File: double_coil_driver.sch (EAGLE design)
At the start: 57 parts, among them Q1 MOSFET-N, Q3 IRF7493, U2 V_REG_LDOSMD, U3 LT3750EMSPBF, X1 COIL

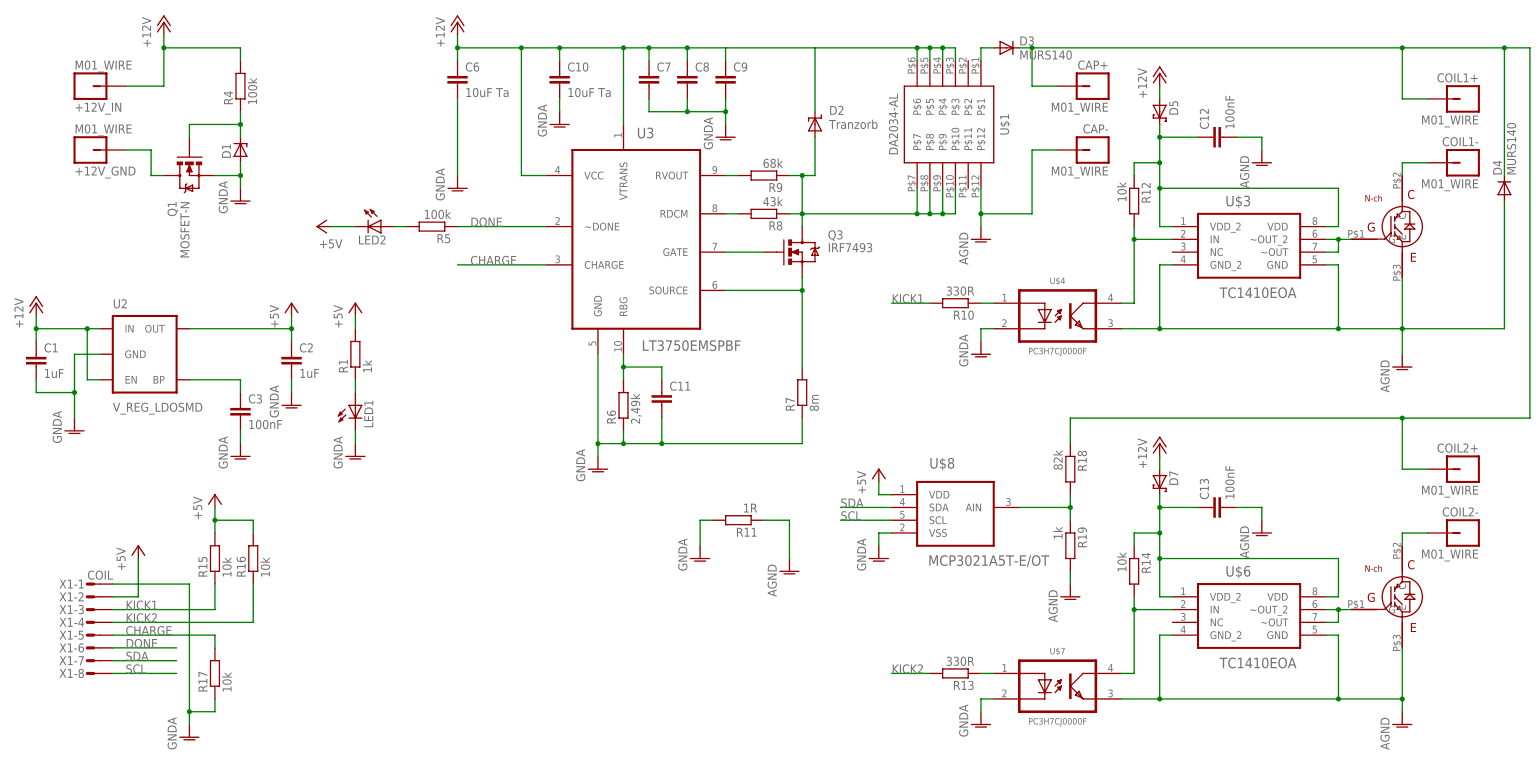
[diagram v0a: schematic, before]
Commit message: Added opamp to ADC, changed board layout a bit
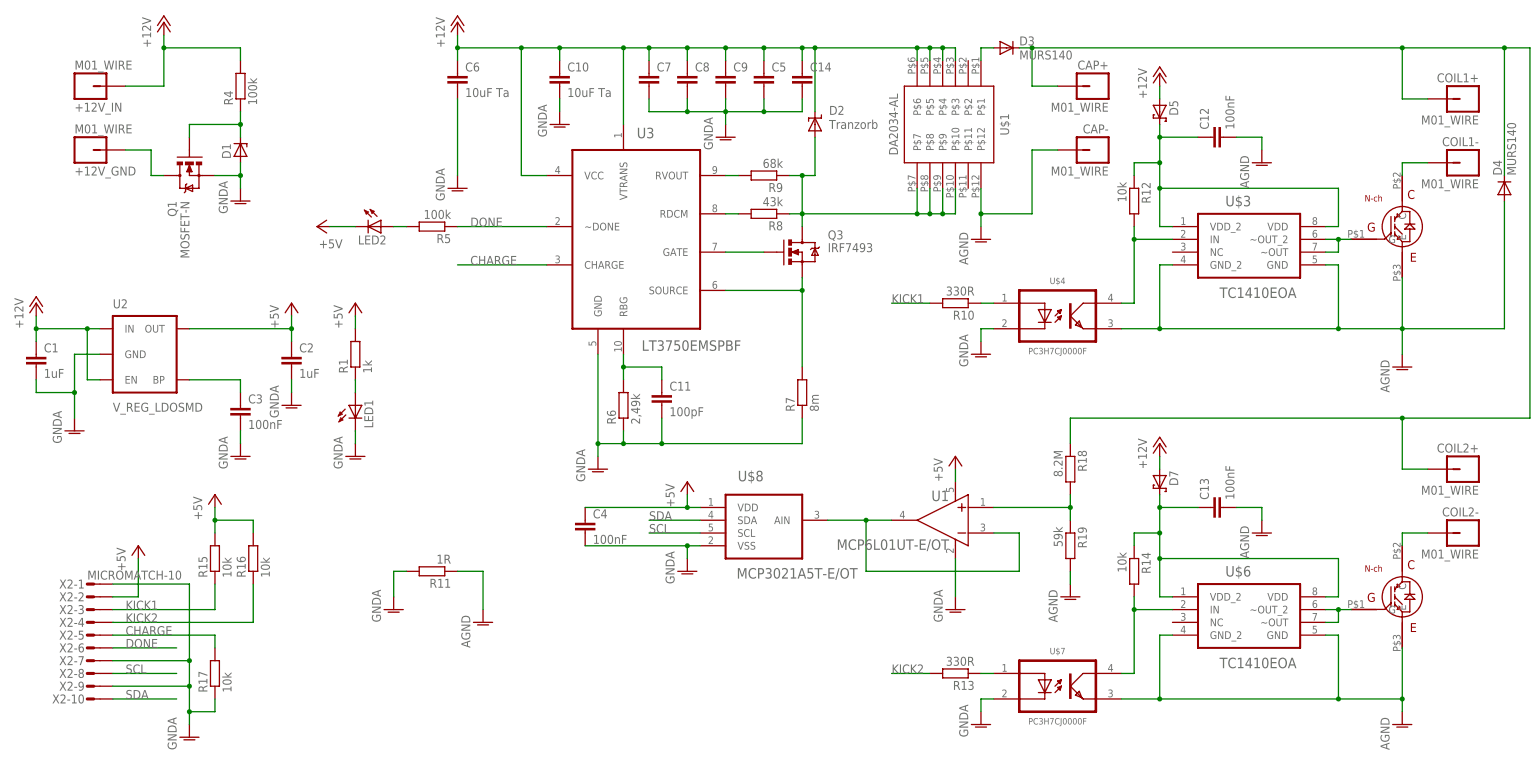
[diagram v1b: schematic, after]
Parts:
- removed X1: COIL, con-amp-micromatch:MICROMATCH-8
- added C14, C5: (no value), rcl:C-EUC1210K
- added C4: 100nF, rcl:C-EUC0603K
- added U1: MCP6L01UT-E/OT, opamp-MCP6L01U:MCP6L01UT-E/OT
- added X2: MICROMATCH-10, con-amp-micromatch:MICROMATCH-10
- C11: value (none) -> 100pF
- R18: value 82k -> 8.2M
- R19: value 1k -> 59k
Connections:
- new net N$5: U$8.AIN, U1.VIN-, U1.VOUT
- net +12V: now also C14.1, C5.1
- net +5V: now also C4.1, U1.VDD, X2-2.S; no longer X1-2.S
- net CHARGE: now also X2-5.S; no longer X1-5.S
- net DONE: now also X2-6.S; no longer X1-6.S
- net GNDA: now also C14.2, C4.2, C5.2, U1.VSS, X2-1.S, X2-7.S, X2-9.S; no longer X1-1.S
- net KICK1: now also X2-3.S; no longer X1-3.S
- net KICK2: now also X2-4.S; no longer X1-4.S
- net N$3: now also U1.VIN+; no longer U$8.AIN
- net SCL: now also X2-8.S; no longer X1-8.S
- net SDA: now also X2-10.S; no longer X1-7.S
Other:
- moved on the sheet: R11, U$8

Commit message: Changed board layout
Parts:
- removed D1: (no value), diode:ZENER-DIODESOD123
- added D6, D8: MURS140, diode:DIODE-DO214AA
- U$2, U$5: device to-247_n-channel_igbt:TO-247A -> to-247_n-channel_igbt-modified-pads:TO-247A
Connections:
- net GNDA: no longer D1.A
- net N$15: now also D6.C, D8.C
- net N$16: now also D6.A
- net N$23: now also D8.A
- net N$7: no longer D1.C
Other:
- moved on the sheet: R4
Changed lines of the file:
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@@
 <part name="GND8" library="supply1" deviceset="GNDA" device=""/>
 <part name="Q1" library="SparkFun-DiscreteSemi" deviceset="MOSFET-NCHANNEL" device="FDS6630A" value="MOSFET-N"/>
-<part name="D1" library="diode" deviceset="ZENER-DIODE" device="SOD123"/>
 <part name="R4" library="rcl" deviceset="R-EU_" device="R0603" value="100k"/>
 <part name="U3" library="LT3750" deviceset="LT3750EMSPBF" device=""/>
@@
 <part name="D3" library="diode" deviceset="DIODE-" device="DO214AA" value="MURS140"/>
 <part name="D4" library="diode" deviceset="DIODE-" device="DO214AA" value="MURS140"/>
-<part name="U$2" library="to-247_n-channel_igbt" deviceset="TO-247" device="A"/>
+<part name="U$2" library="to-247_n-channel_igbt-modified-pads" deviceset="TO-247" device="A"/>
 <part name="U$3" library="TC1410" deviceset="TC1410EOA" device=""/>
 <part name="U$4" library="optocoupler-PC3H7CJ0000F" deviceset="PC3H7CJ0000F" device=""/>
@@
 <part name="P+10" library="supply1" deviceset="+12V" device=""/>
 <part name="C12" library="rcl" deviceset="C-EU" device="C0603K" value="100nF"/>
-<part name="U$5" library="to-247_n-channel_igbt" deviceset="TO-247" device="A"/>
+<part name="U$5" library="to-247_n-channel_igbt-modified-pads" deviceset="TO-247" device="A"/>
 <part name="U$6" library="TC1410" deviceset="TC1410EOA" device=""/>
 <part name="U$7" library="optocoupler-PC3H7CJ0000F" deviceset="PC3H7CJ0000F" device=""/>
@@
 <part name="C14" library="rcl" deviceset="C-EU" device="C1210K"/>
 <part name="X2" library="con-amp-micromatch" deviceset="MICROMATCH-10" device=""/>
+<part name="D6" library="diode" deviceset="DIODE-" device="DO214AA" value="MURS140"/>
+<part name="D8" library="diode" deviceset="DIODE-" device="DO214AA" value="MURS140"/>
 </parts>
 <sheets>
@@
 <instance part="GND8" gate="1" x="58.42" y="127"/>
 <instance part="Q1" gate="G$1" x="48.26" y="132.08" rot="MR270"/>
-<instance part="D1" gate="G$1" x="58.42" y="137.16" rot="R90"/>
-<instance part="R4" gate="G$1" x="58.42" y="149.86" rot="R90"/>
+<instance part="R4" gate="G$1" x="48.26" y="149.86" rot="R90"/>
 <instance part="U3" gate="A" x="137.16" y="121.92"/>
 <instance part="Q3" gate="G$1" x="170.18" y="116.84"/>
@@
 <instance part="X2" gate="-9" x="27.94" y="30.48"/>
 <instance part="X2" gate="-10" x="27.94" y="27.94"/>
+<instance part="D6" gate="G$1" x="284.48" y="139.7" rot="R90"/>
+<instance part="D8" gate="G$1" x="284.48" y="66.04" rot="R90"/>
 </instances>
 <busses>
@@
 <pinref part="GND8" gate="1" pin="GNDA"/>
 <wire x1="58.42" y1="129.54" x2="58.42" y2="132.08" width="0.1524" layer="91"/>
-<pinref part="D1" gate="G$1" pin="A"/>
-<wire x1="58.42" y1="134.62" x2="58.42" y2="132.08" width="0.1524" layer="91"/>
-<junction x="58.42" y="132.08"/>
 </segment>
 <segment>
@@
 <pinref part="R4" gate="G$1" pin="2"/>
 <wire x1="43.18" y1="157.48" x2="43.18" y2="160.02" width="0.1524" layer="91"/>
-<wire x1="58.42" y1="154.94" x2="58.42" y2="157.48" width="0.1524" layer="91"/>
-<wire x1="58.42" y1="157.48" x2="43.18" y2="157.48" width="0.1524" layer="91"/>
+<wire x1="48.26" y1="154.94" x2="48.26" y2="157.48" width="0.1524" layer="91"/>
+<wire x1="48.26" y1="157.48" x2="43.18" y2="157.48" width="0.1524" layer="91"/>
 <junction x="43.18" y="157.48"/>
 </segment>
@@
 <net name="N$7" class="0">
 <segment>
-<pinref part="D1" gate="G$1" pin="C"/>
 <pinref part="R4" gate="G$1" pin="1"/>
-<wire x1="58.42" y1="139.7" x2="58.42" y2="142.24" width="0.1524" layer="91"/>
 <pinref part="Q1" gate="G$1" pin="G"/>
-<wire x1="58.42" y1="142.24" x2="58.42" y2="144.78" width="0.1524" layer="91"/>
-<wire x1="48.26" y1="139.7" x2="48.26" y2="142.24" width="0.1524" layer="91"/>
-<wire x1="48.26" y1="142.24" x2="58.42" y2="142.24" width="0.1524" layer="91"/>
-<junction x="58.42" y="142.24"/>
+<wire x1="48.26" y1="139.7" x2="48.26" y2="144.78" width="0.1524" layer="91"/>
 </segment>
 </net>
@@
 <pinref part="R18" gate="G$1" pin="1"/>
 <wire x1="223.52" y1="78.74" x2="223.52" y2="83.82" width="0.1524" layer="91"/>
+<pinref part="D8" gate="G$1" pin="C"/>
+<wire x1="284.48" y1="68.58" x2="284.48" y2="73.66" width="0.1524" layer="91"/>
+<wire x1="284.48" y1="73.66" x2="289.56" y2="73.66" width="0.1524" layer="91"/>
+<junction x="289.56" y="73.66"/>
+<pinref part="D6" gate="G$1" pin="C"/>
+<wire x1="284.48" y1="142.24" x2="284.48" y2="147.32" width="0.1524" layer="91"/>
+<wire x1="284.48" y1="147.32" x2="289.56" y2="147.32" width="0.1524" layer="91"/>
+<junction x="289.56" y="147.32"/>
 </segment>
 </net>
@@
 <wire x1="289.56" y1="134.62" x2="294.64" y2="134.62" width="0.1524" layer="91"/>
 <pinref part="COIL1-" gate="G$1" pin="P$1"/>
+<pinref part="D6" gate="G$1" pin="A"/>
+<wire x1="284.48" y1="137.16" x2="284.48" y2="134.62" width="0.1524" layer="91"/>
+<wire x1="284.48" y1="134.62" x2="289.56" y2="134.62" width="0.1524" layer="91"/>
+<junction x="289.56" y="134.62"/>
 </segment>
 </net>
@@
 <wire x1="289.56" y1="60.96" x2="294.64" y2="60.96" width="0.1524" layer="91"/>
 <pinref part="COIL2-" gate="G$1" pin="P$1"/>
-</segment>
-</net>
+<pinref part="D8" gate="G$1" pin="A"/>
+<wire x1="284.48" y1="63.5" x2="284.48" y2="60.96" width="0.1524" layer="91"/>
+<wire x1="284.48" y1="60.96" x2="289.56" y2="60.96" width="0.1524" layer="91"/>
+<junction x="289.56" y="60.96"/>
+</segment>
+</net>

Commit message: Added missing capacitor values
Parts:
- C14, C5, C7, C8, C9: value (none) -> 10uF
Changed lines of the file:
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@@
 <part name="COIL2+" library="tellis2" deviceset="M01_WIRE" device=""/>
 <part name="COIL2-" library="tellis2" deviceset="M01_WIRE" device=""/>
-<part name="C7" library="rcl" deviceset="C-EU" device="C1210K"/>
-<part name="C8" library="rcl" deviceset="C-EU" device="C1210K"/>
-<part name="C9" library="rcl" deviceset="C-EU" device="C1210K"/>
+<part name="C7" library="rcl" deviceset="C-EU" device="C1210K" value="10uF"/>
+<part name="C8" library="rcl" deviceset="C-EU" device="C1210K" value="10uF"/>
+<part name="C9" library="rcl" deviceset="C-EU" device="C1210K" value="10uF"/>
 <part name="C1" library="rcl" deviceset="C-EU" device="C1206K" value="1uF"/>
 <part name="C2" library="rcl" deviceset="C-EU" device="C1206K" value="1uF"/>
@@
 <part name="U1" library="opamp-MCP6L01U" deviceset="MCP6L01UT-E/OT" device=""/>
 <part name="C4" library="rcl" deviceset="C-EU" device="C0603K" value="100nF"/>
-<part name="C5" library="rcl" deviceset="C-EU" device="C1210K"/>
-<part name="C14" library="rcl" deviceset="C-EU" device="C1210K"/>
+<part name="C5" library="rcl" deviceset="C-EU" device="C1210K" value="10uF"/>
+<part name="C14" library="rcl" deviceset="C-EU" device="C1210K" value="10uF"/>
 <part name="X2" library="con-amp-micromatch" deviceset="MICROMATCH-10" device=""/>
 <part name="D6" library="diode" deviceset="DIODE-" device="DO214AA" value="MURS140"/>

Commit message: Changed kick pull-ups to pull-downs
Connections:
- net +5V: no longer R15.2, R16.2
- net GNDA: now also R15.1, R16.1
- net KICK1: now also R16.2; no longer R15.1
- net KICK2: now also R15.2; no longer R16.1
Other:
- moved on the sheet: R15, R16
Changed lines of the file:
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@@
 <?xml version="1.0" encoding="utf-8"?>
 <!DOCTYPE eagle SYSTEM "eagle.dtd">
-<eagle version="6.5.0">
+<eagle version="7.0.0">
 <drawing>
 <settings>
@@
 <instance part="P+11" gate="1" x="241.3" y="78.74"/>
 <instance part="C13" gate="G$1" x="251.46" y="66.04" rot="R90"/>
-<instance part="R15" gate="G$1" x="53.34" y="55.88" rot="R90"/>
-<instance part="R16" gate="G$1" x="60.96" y="55.88" rot="R90"/>
+<instance part="R15" gate="G$1" x="60.96" y="33.02" rot="R90"/>
+<instance part="R16" gate="G$1" x="68.58" y="33.02" rot="R90"/>
 <instance part="R17" gate="G$1" x="53.34" y="33.02" rot="R90"/>
 <instance part="CAP+" gate="G$1" x="228.6" y="149.86"/>
@@
 <junction x="48.26" y="30.48"/>
 <junction x="48.26" y="35.56"/>
+<pinref part="R15" gate="G$1" pin="1"/>
+<wire x1="60.96" y1="27.94" x2="60.96" y2="25.4" width="0.1524" layer="91"/>
+<wire x1="60.96" y1="25.4" x2="53.34" y2="25.4" width="0.1524" layer="91"/>
+<pinref part="R16" gate="G$1" pin="1"/>
+<wire x1="68.58" y1="27.94" x2="68.58" y2="25.4" width="0.1524" layer="91"/>
+<wire x1="68.58" y1="25.4" x2="60.96" y2="25.4" width="0.1524" layer="91"/>
+<junction x="53.34" y="25.4"/>
+<junction x="60.96" y="25.4"/>
 </segment>
 <segment>
@@
 <pinref part="P+8" gate="1" pin="+5V"/>
 <wire x1="76.2" y1="121.92" x2="81.28" y2="121.92" width="0.1524" layer="91"/>
-</segment>
-<segment>
-<pinref part="R16" gate="G$1" pin="2"/>
-<wire x1="60.96" y1="63.5" x2="60.96" y2="60.96" width="0.1524" layer="91"/>
-<pinref part="R15" gate="G$1" pin="2"/>
-<wire x1="53.34" y1="66.04" x2="53.34" y2="63.5" width="0.1524" layer="91"/>
-<wire x1="53.34" y1="63.5" x2="53.34" y2="60.96" width="0.1524" layer="91"/>
-<wire x1="53.34" y1="63.5" x2="60.96" y2="63.5" width="0.1524" layer="91"/>
-<junction x="53.34" y="63.5"/>
-<pinref part="P+6" gate="1" pin="+5V"/>
 </segment>
 <segment>
@@
 <segment>
 <label x="35.56" y="45.72" size="1.778" layer="95"/>
-<wire x1="33.02" y1="45.72" x2="53.34" y2="45.72" width="0.1524" layer="91"/>
-<pinref part="R15" gate="G$1" pin="1"/>
-<wire x1="53.34" y1="45.72" x2="53.34" y2="50.8" width="0.1524" layer="91"/>
+<wire x1="33.02" y1="45.72" x2="68.58" y2="45.72" width="0.1524" layer="91"/>
 <pinref part="X2" gate="-3" pin="S"/>
+<pinref part="R16" gate="G$1" pin="2"/>
+<wire x1="68.58" y1="45.72" x2="68.58" y2="38.1" width="0.1524" layer="91"/>
 </segment>
 </net>
@@
 <label x="35.56" y="43.18" size="1.778" layer="95"/>
 <wire x1="33.02" y1="43.18" x2="60.96" y2="43.18" width="0.1524" layer="91"/>
-<pinref part="R16" gate="G$1" pin="1"/>
-<wire x1="60.96" y1="43.18" x2="60.96" y2="50.8" width="0.1524" layer="91"/>
 <pinref part="X2" gate="-4" pin="S"/>
+<pinref part="R15" gate="G$1" pin="2"/>
+<wire x1="60.96" y1="43.18" x2="60.96" y2="38.1" width="0.1524" layer="91"/>
 </segment>
 </net>
